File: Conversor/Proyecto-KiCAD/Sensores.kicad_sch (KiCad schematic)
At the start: 23 parts

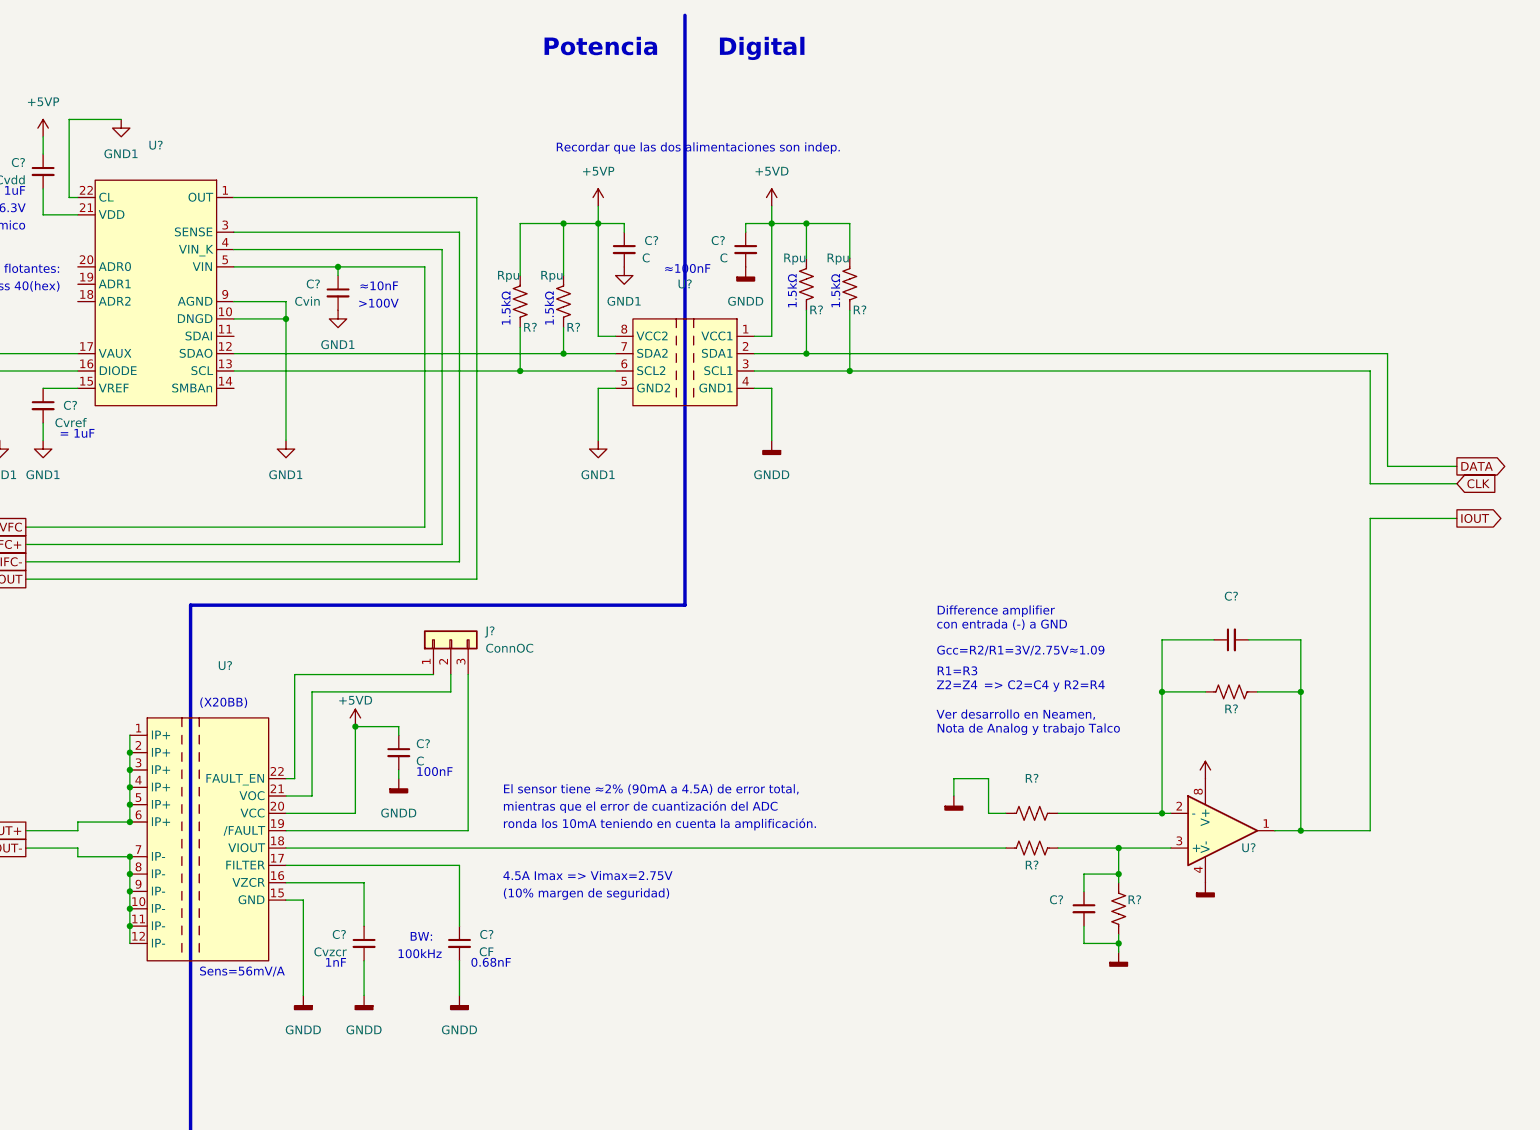
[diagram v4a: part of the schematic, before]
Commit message: Completar las fuentes aisladas del lado digital
- Falta hacer las fuentes del lado de potencia (sin las TRACO).
  - Se tiene que tomar la entrada de 12V-18V y pasarla por un regulador de 15V.
  - Despues esa salida de 15V se pasa por un regulador que la baje a 5V.
- Agregadas datasheets y notas:
  - Datasheets de regulador LM1117 para pasar de 5V a 3.3V para alimentar el DSP.
  - Notas de aplicacion de la fuente TRACO y explicaciones de corrientes sink y source.
- Hay que ver las cosas que me tiene que pasar Jorge de la alimentacion del DSP.
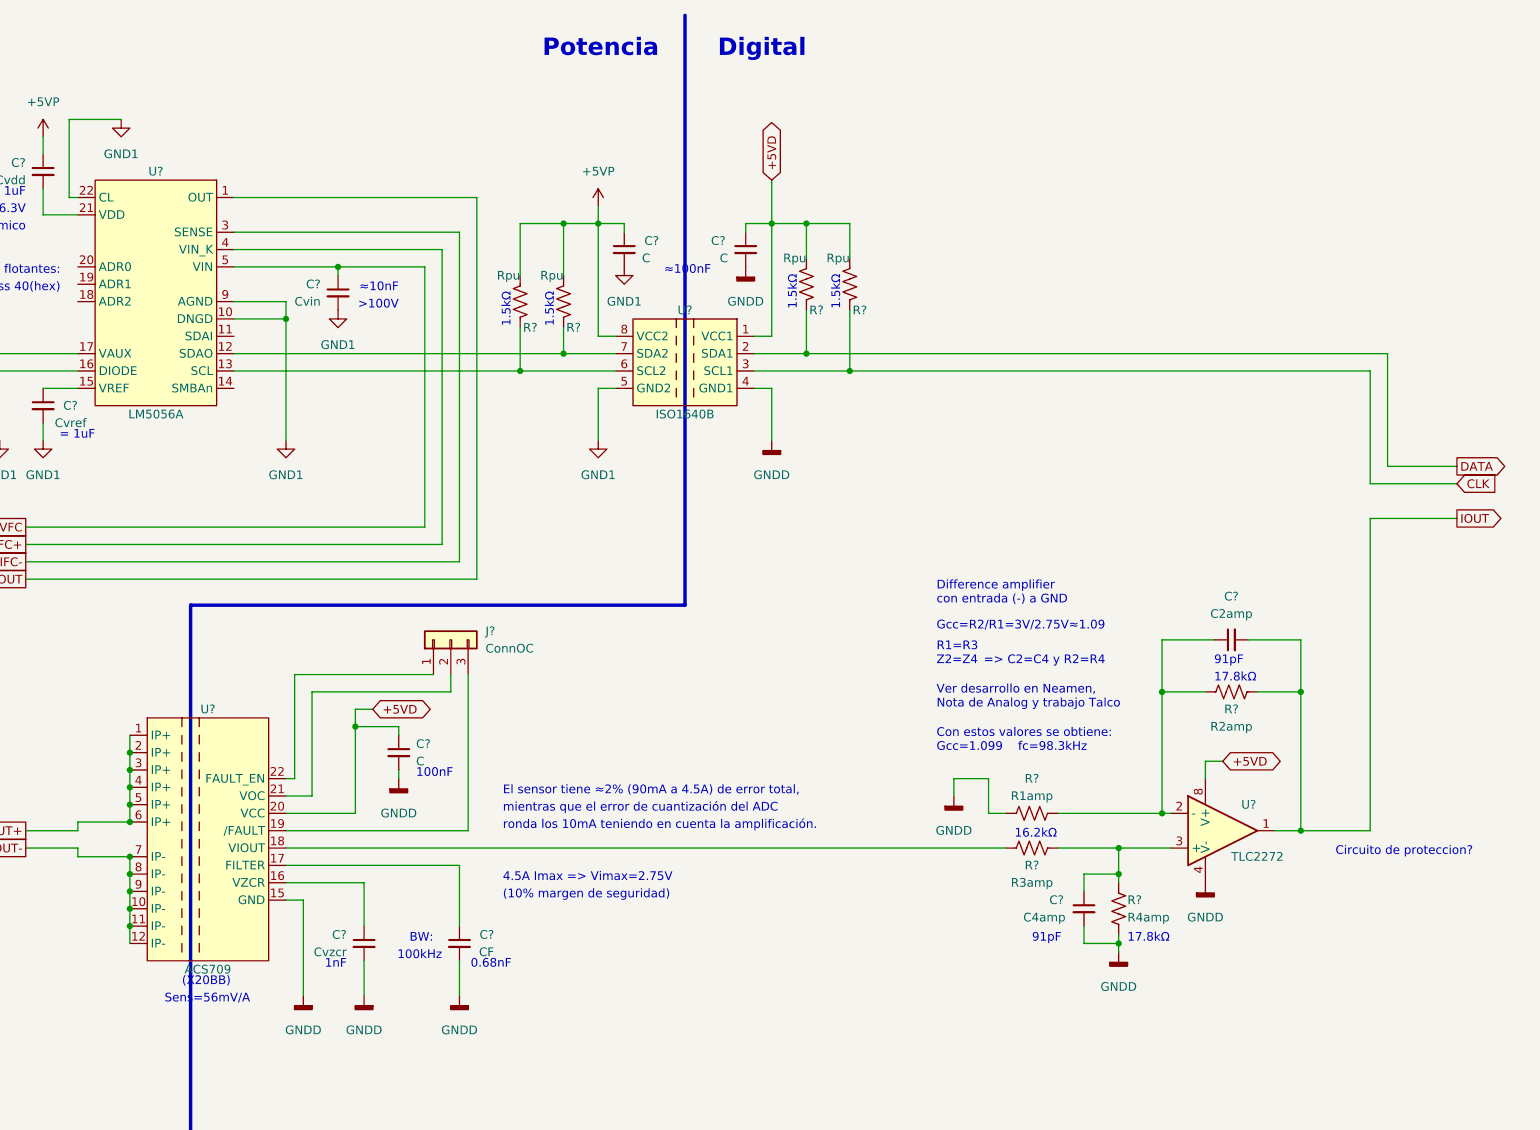
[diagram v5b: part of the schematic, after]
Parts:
- C?: value (none) -> C2amp
- C?: value (none) -> C4amp
- R?: value (none) -> R4amp
- R?: value (none) -> R2amp
- R?: value (none) -> R3amp
- R?: value (none) -> R1amp
- U?: value (none) -> TLC2272; footprint (none) -> Package_SO:SOIC-8_3.9x4.9mm_P1.27mm
- U?: value (none) -> ACS709; footprint (none) -> Package_SO:SSOP-24_3.9x8.7mm_P0.635mm
- U?: value (none) -> LM5056A; footprint (none) -> Package_SO:HTSSOP-28-1EP_4.4x9.7mm_P0.65mm_EP2.85x5.4mm_ThermalVias
- U?: value (none) -> ISO1640B; footprint (none) -> Package_SO:SOIC-8_3.9x4.9mm_P1.27mm
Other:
- note added: "16.2kΩ"
- note added: "17.8kΩ"
- note added: "91pF"
- note added: "Circuito de proteccion?"
- note added: "Con estos valores se obtiene: Gcc=1.099 fc=98.3kHz"
- note removed: "Recordar que las dos alimentaciones son indep."

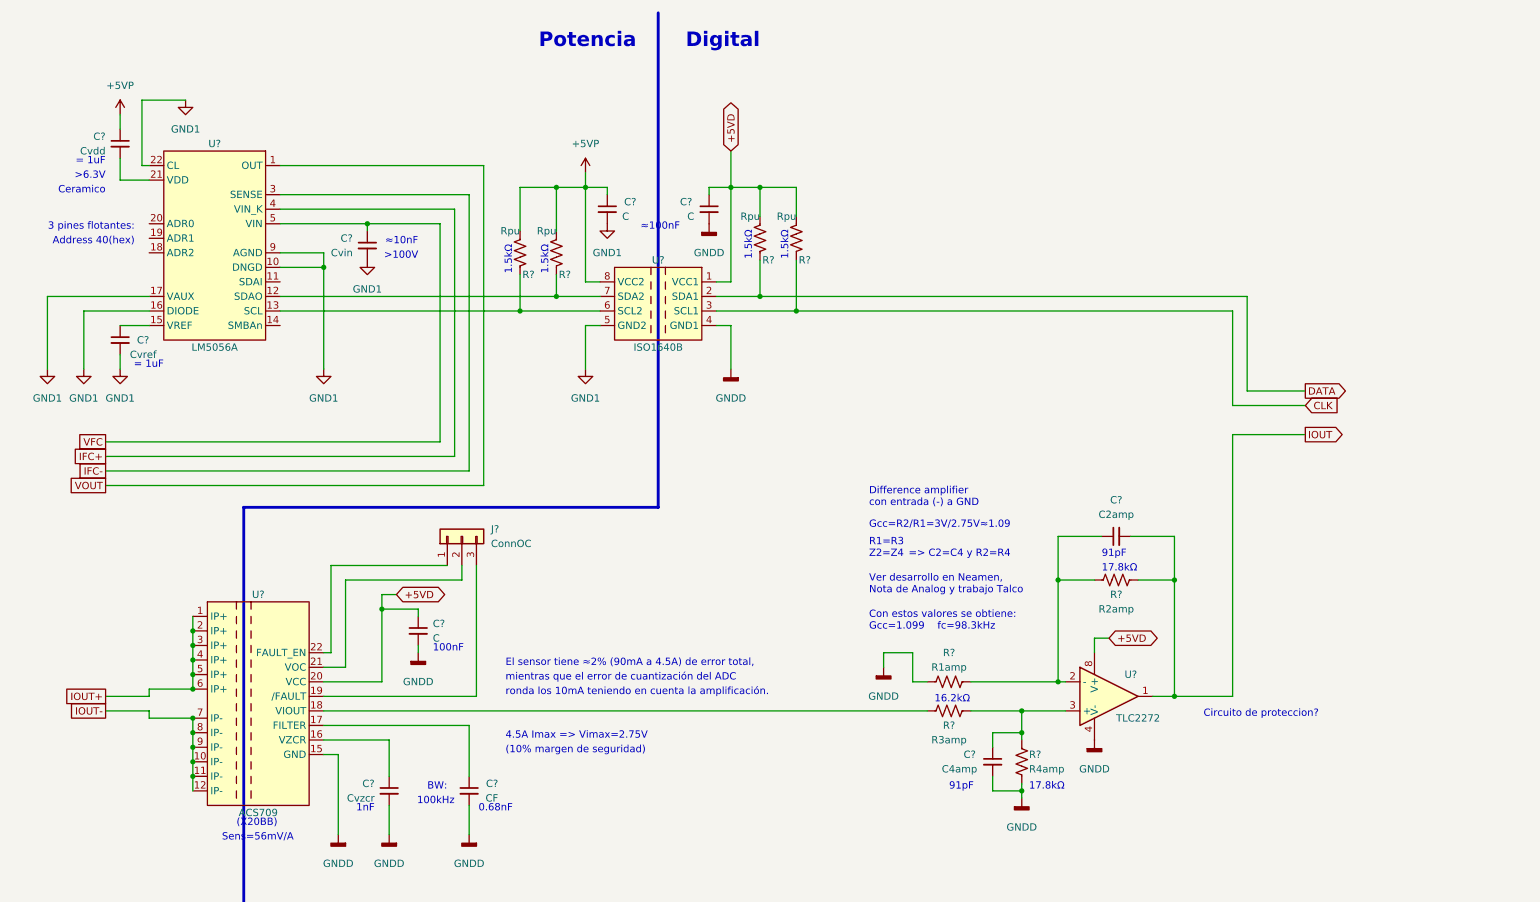
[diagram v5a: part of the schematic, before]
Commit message: Modificar las fuentes de alimentacion
- Falta la fuente regulada de 15V para Vdd de los drivers (Sale a partir de alimentacion de 24V?)
- El DSP se alimenta por +5V a traves de la placa de prueba
- 3.3V para la proteccion a la salida del AO del ACS709
- Agregada datasheet del regulador MC7805 de 12-18V a 5VP
- Uso el pin de dead-time (DT) de los drivers para evitar corto en una pata del
  puente de MOSFETs (200ns de dead-time)
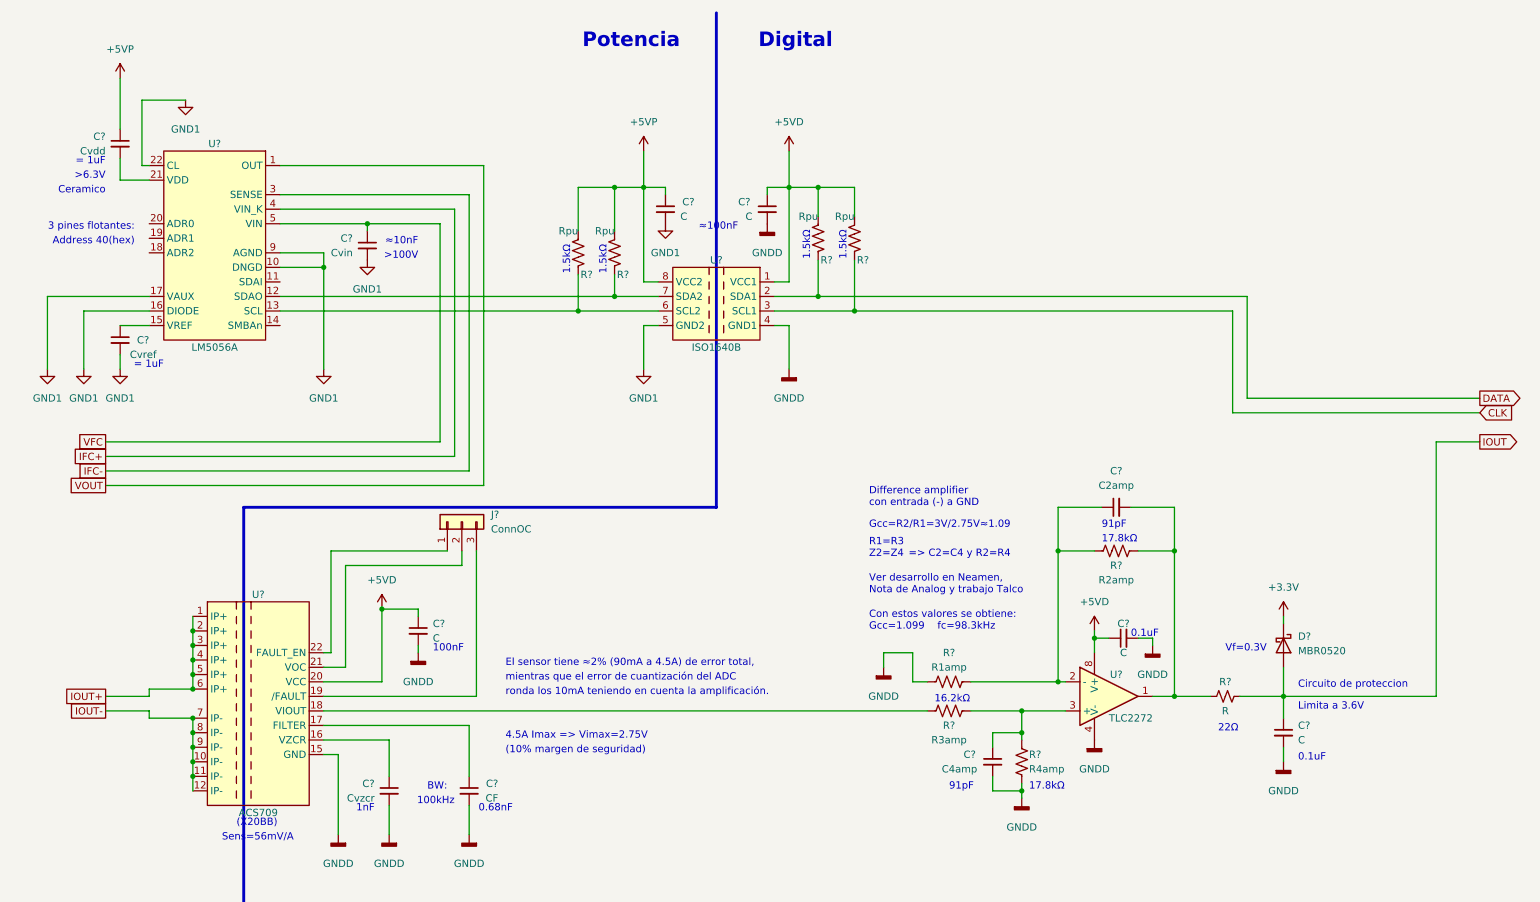
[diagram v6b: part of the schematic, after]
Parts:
- added C? (x2): C, symbol Device:C_Small
- added D?: MBR0520, Diode_SMD:D_SOD-123, symbol Diode:MBR0520
- added R?: R, symbol Device:R_Small_US
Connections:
- net +5VD: now also C?.1
- net GNDD: now also C?.2, C?.2
- net IOUT: now also C?.1, D?.2 (A), R?.2; no longer C?.2, R?.2, U?.1
- new net: C?.2, R?.1, R?.2, U?.1
- new net +3V3: D?.1 (K)
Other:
- note added: "0.1uF"
- note added: "22Ω"
- note added: "Circuito de proteccion"
- note added: "Limita a 3.6V"
- note added: "Vf=0.3V"
- note removed: "Circuito de proteccion?"
- moved on the sheet: C?, J?, R?, U?

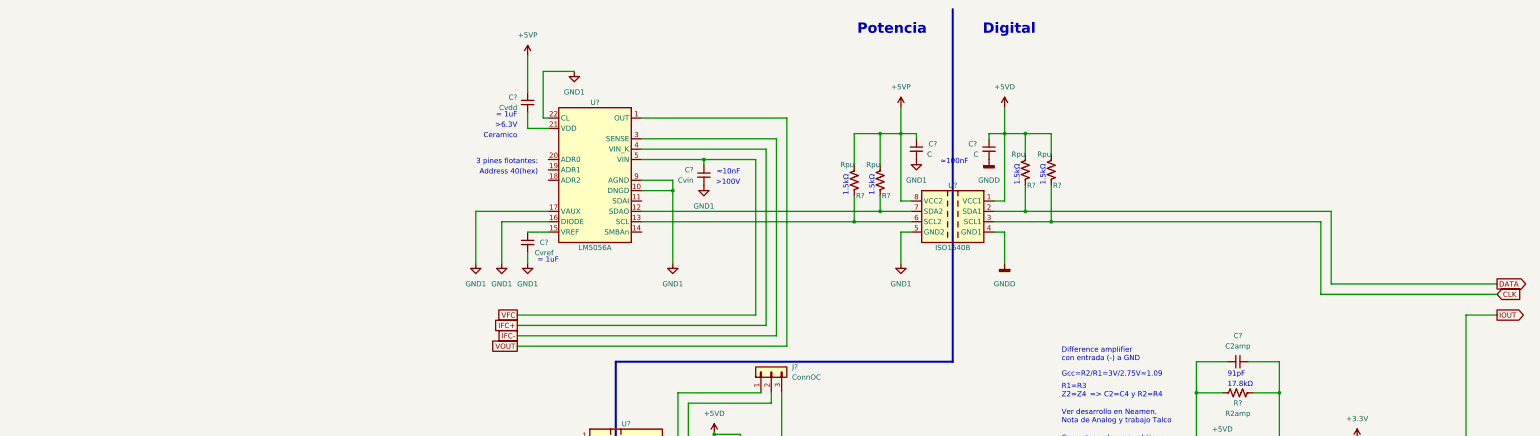
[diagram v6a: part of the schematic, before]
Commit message: Cambiar	drivers	por ADuM4221 de	Analog y completar alimentacion
- UCC21540 y UCC27200 sin stock:
	- Reemplazado por el ADuM4221/ADuM4221-1 de Analog, que es muy similar
	- Alternativa el LTC7061, que tiene DT pero no es aislado
- Aisladores sin stock, falta buscar un reemplazo
- Agregadas las hojas de datos
- LM5056A con poco stock (Hay que comprar muy pronto)
- Completada la lista de componentes con todos los integrados/diodos/transistores
- Agregada nota de aplicacion sobre peak source y sink current
- Agregadas bibliotecas del ADuM4421 y LM5056A bajadas de las paginas de Analog y TI respectivamente
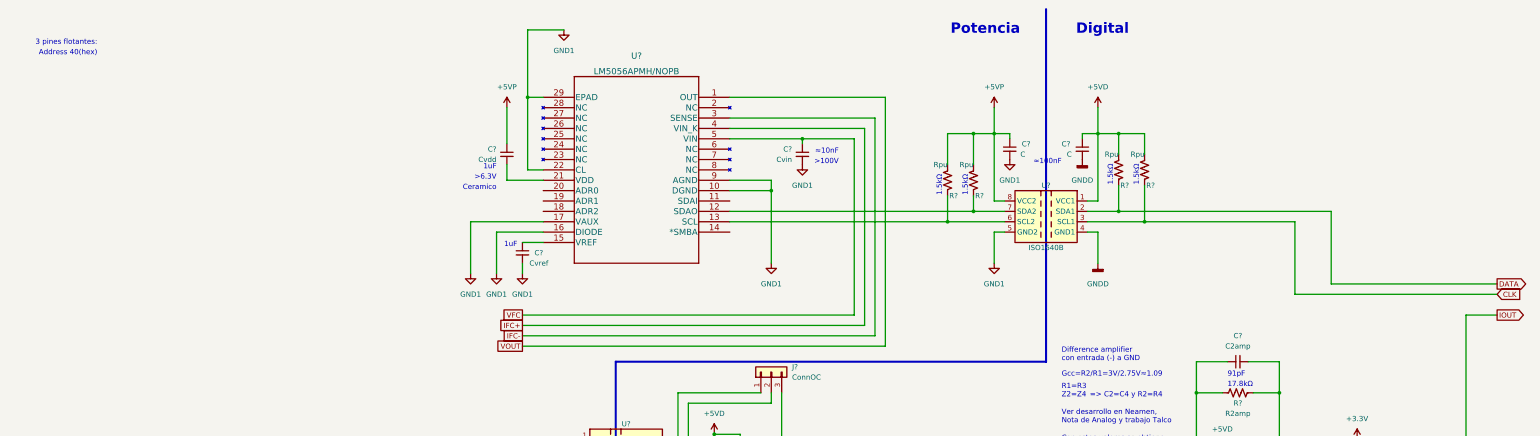
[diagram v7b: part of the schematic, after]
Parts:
- removed U?: LM5056A, Package_SO:HTSSOP-28-1EP_4.4x9.7mm_P0.65mm_EP2.85x5.4mm_ThermalVias, symbol Componentes proyecto:LM5056A
- added U?: LM5056APMH/NOPB, PWP28_TEX, symbol 2022-05-17_17-00-40:LM5056APMH/NOPB
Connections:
- net GND1: now also U?.10 (DGND), U?.16 (DIODE), U?.17 (VAUX), U?.22 (CL), U?.29 (EPAD), U?.9 (AGND)
- net IFC+: now also U?.4 (VIN_K)
- net IFC-: now also U?.3 (SENSE)
- net VFC: now also U?.5 (VIN)
- net VOUT: now also U?.1 (OUT)
- net at R?.2, U?.6 (SCL2): now also U?.13 (SCL)
- net at R?.2, U?.7 (SDA2): now also U?.12 (SDAO)
- net at C?.1: now also U?.15 (VREF)
- net at C?.2: now also U?.21 (VDD)
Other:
- note added: "1uF"
- note removed: "= 1uF"
- moved on the sheet: C?, R?, U?
